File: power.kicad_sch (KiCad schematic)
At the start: 27 parts, among them U21 TPS62A06DRLR, U22 INA228AQDGSRQ1, U23 INA187A2IDBVR

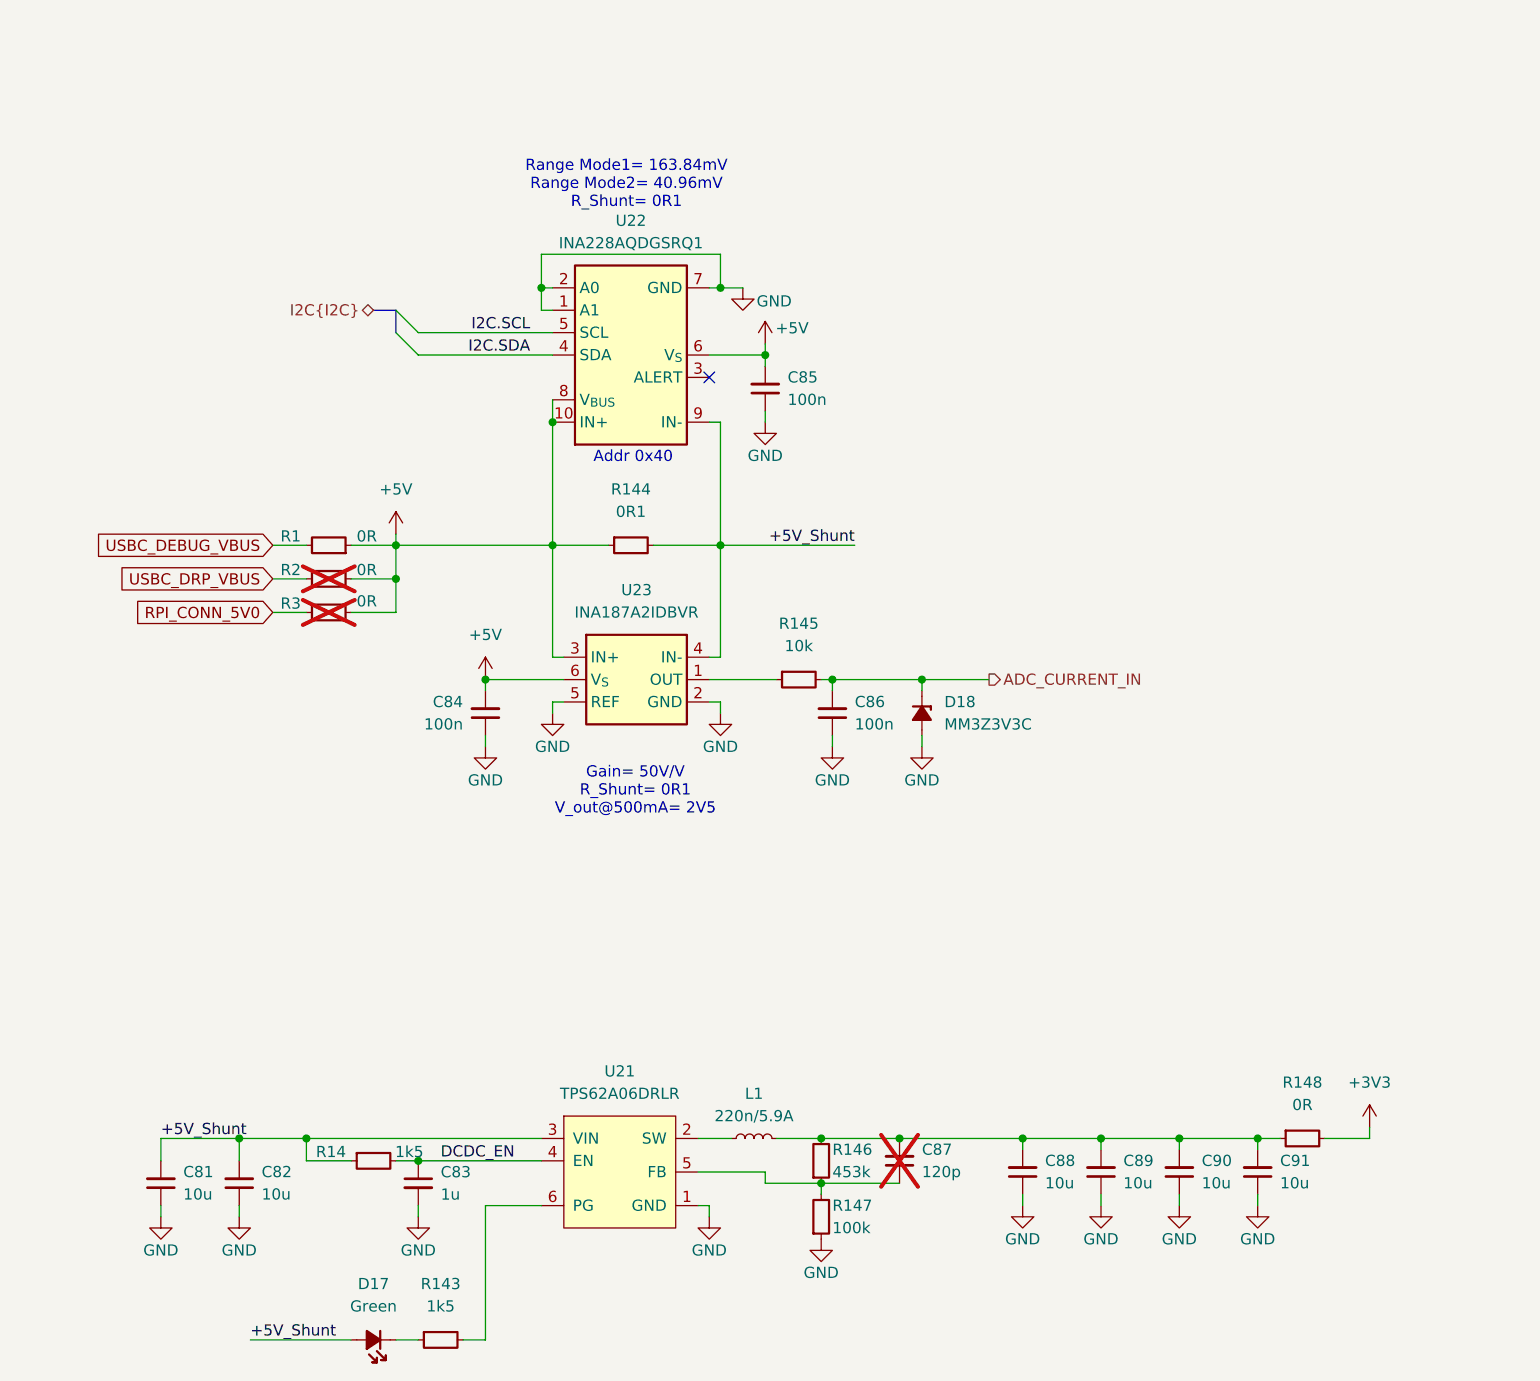
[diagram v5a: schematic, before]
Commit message: [#95036] Solve basic ERCs
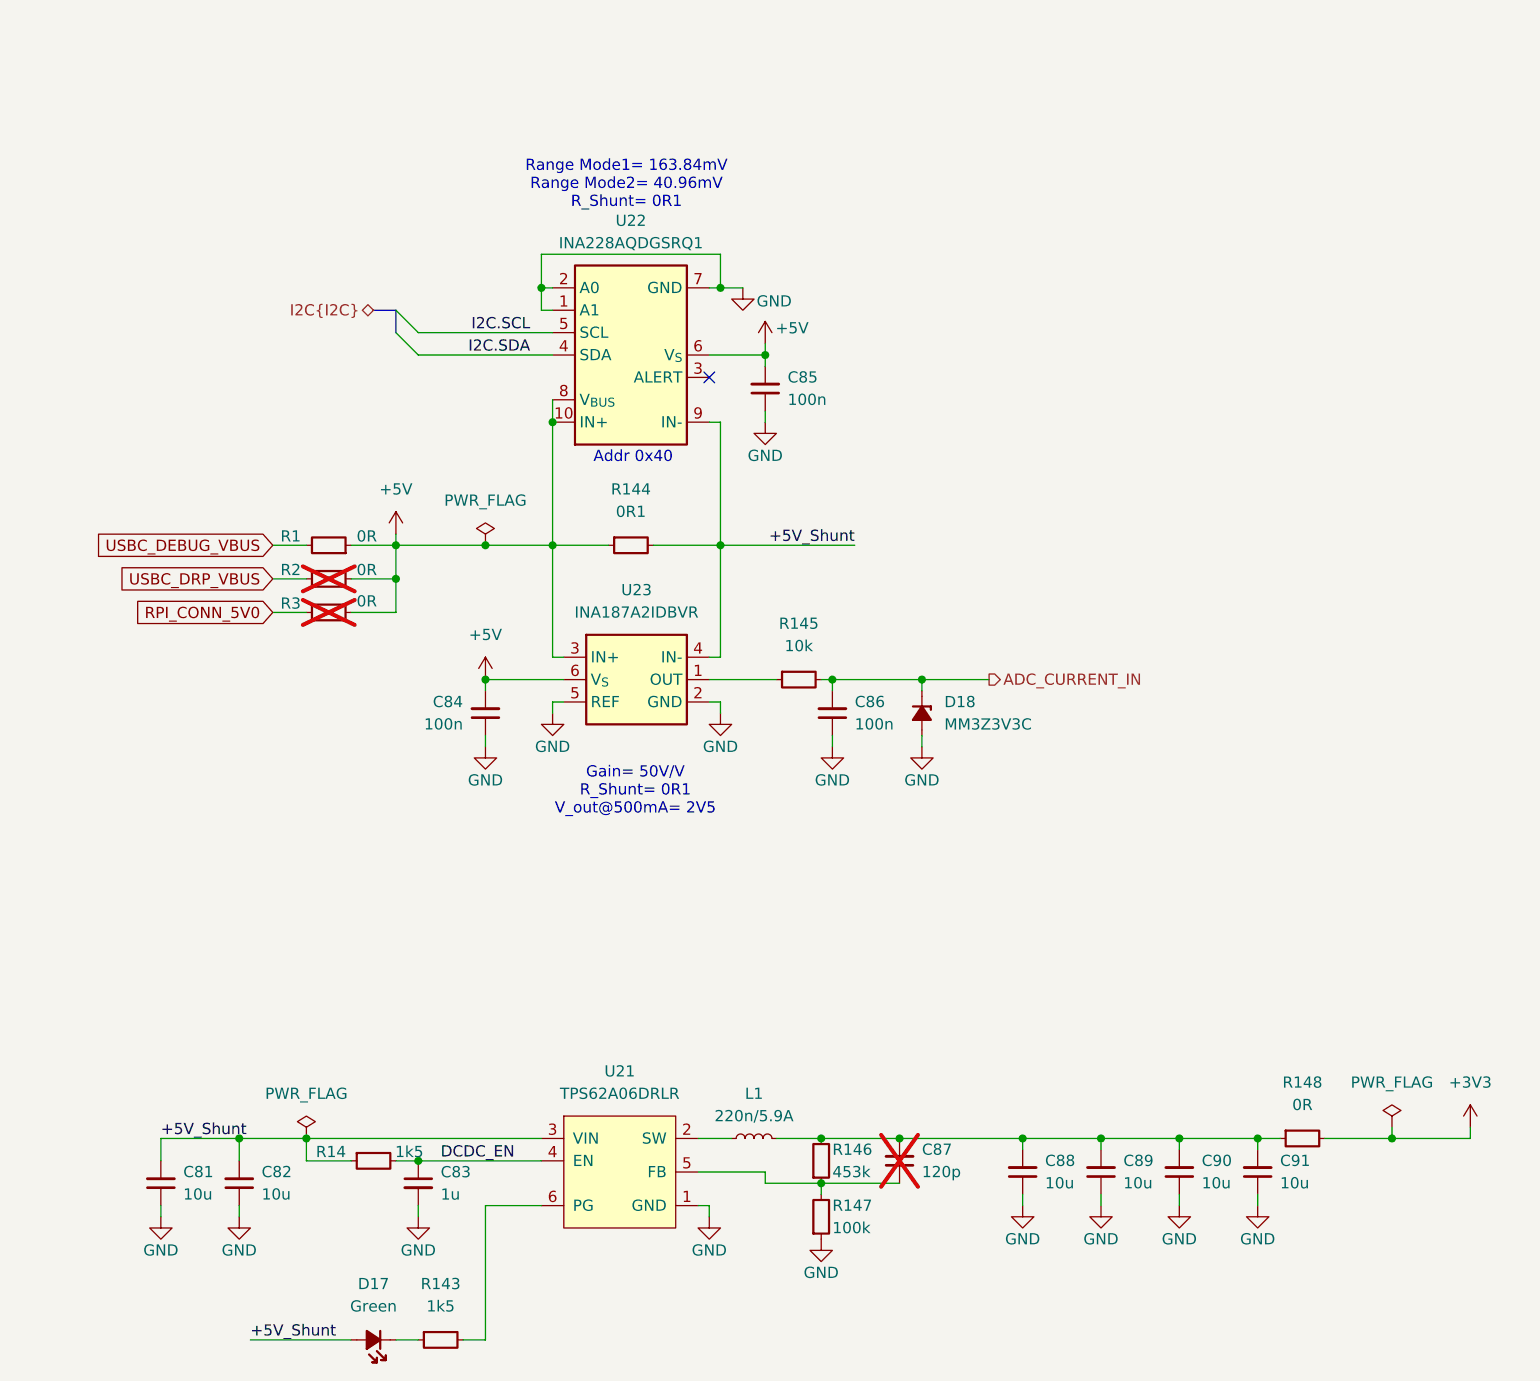
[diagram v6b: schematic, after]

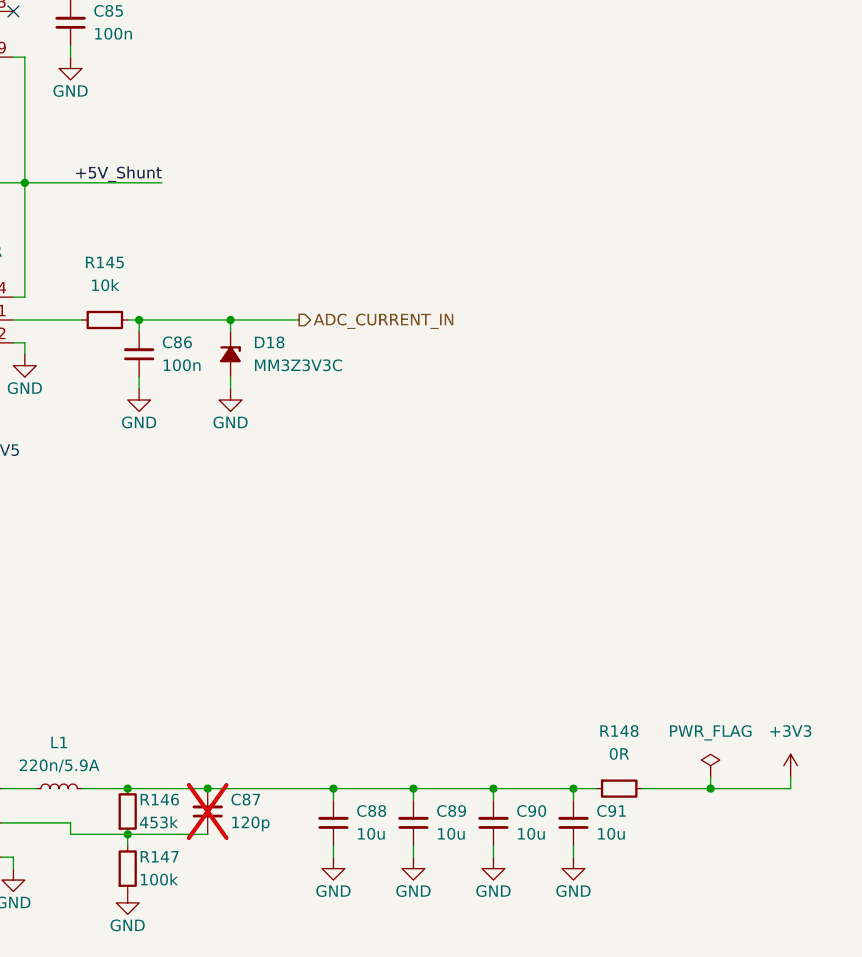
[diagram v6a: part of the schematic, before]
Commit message: [#95036] Add testpoints
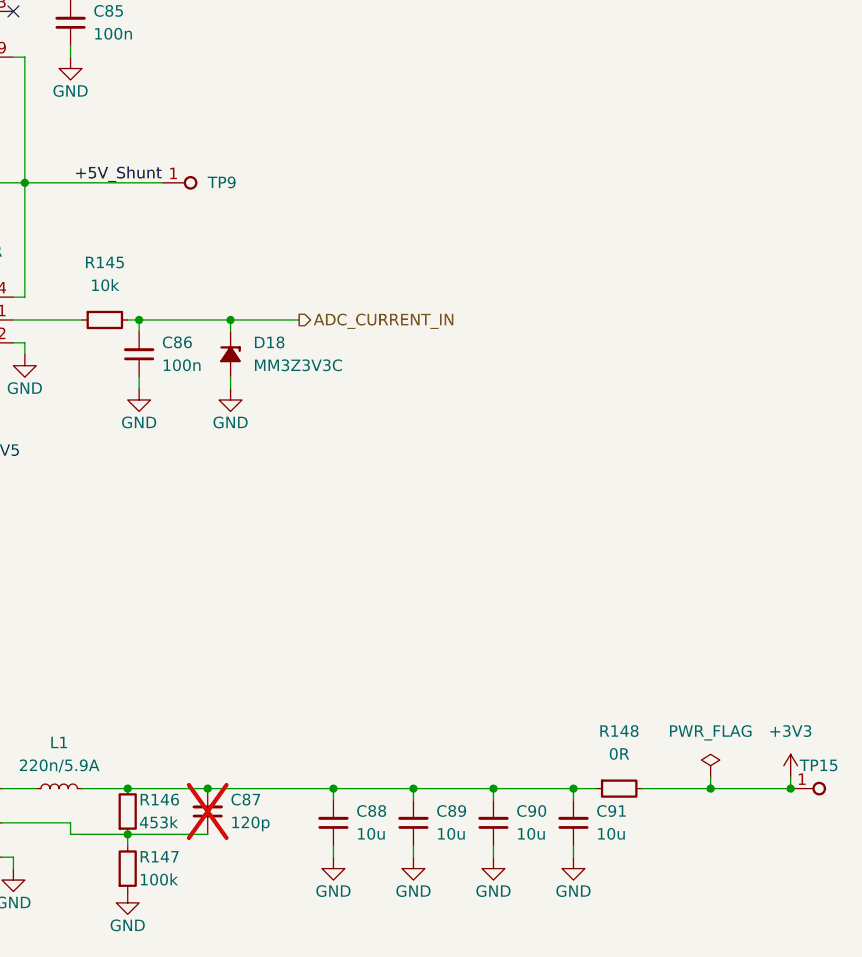
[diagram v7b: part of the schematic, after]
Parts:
- added TP15, TP9: TP_1mm_SMD, antmicro-footprints:TP_SMD_1mm, symbol antmicroTestPoints:TP_1mm_SMD
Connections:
- net +3V3: now also TP15.1
- net +5V_Shunt: now also TP9.1
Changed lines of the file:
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@@
 	)
 	(junction
+		(at 278.13 177.8)
+		(diameter 0)
+		(color 0 0 0 0)
+	)
+	(junction
 		(at 166.37 110.49)
 		(diameter 0)
@@
 	)
 	(symbol
+		(lib_id "antmicroTestPoints:TP_1mm_SMD")
+		(at 278.13 177.8 0)
+		(mirror x)
+		(unit 1)
+		(exclude_from_sim no)
+		(in_bom no)
+		(on_board yes)
+		(dnp no)
+		(property "Reference" "TP15"
+			(at 281.305 175.26 0)
+			(effects
+				(font
+					(size 1.27 1.27)
+					(thickness 0.15)
+				)
+			)
+		)
+		(property "Value" "TP_1mm_SMD"
+			(at 293.37 170.18 0)
+			(effects
+				(font
+					(size 1.27 1.27)
+					(thickness 0.15)
+				)
+				(justify left bottom)
+				(hide yes)
+			)
+		)
+		(property "Footprint" "antmicro-footprints:TP_SMD_1mm"
+			(at 293.37 167.64 0)
+			(effects
+				(font
+					(size 1.27 1.27)
+					(thickness 0.15)
+				)
+				(justify left bottom)
+				(hide yes)
+			)
+		)
+		(property "Datasheet" ""
+			(at 295.91 165.1 0)
+			(effects
+				(font
+					(size 1.27 1.27)
+					(thickness 0.15)
+				)
+				(justify left bottom)
+				(hide yes)
+			)
+		)
+		(property "Description" "Test point 1mm SMD"
+			(at 293.37 157.48 0)
+			(effects
+				(font
+					(size 1.27 1.27)
+				)
+				(justify left bottom)
+				(hide yes)
+			)
+		)
+		(property "MPN" ""
+			(at 278.13 177.8 0)
+			(effects
+				(font
+					(size 1.27 1.27)
+				)
+				(hide yes)
+			)
+		)
+		(property "Manufacturer" ""
+			(at 278.13 177.8 0)
+			(effects
+				(font
+					(size 1.27 1.27)
+				)
+				(hide yes)
+			)
+		)
+		(property "Author" "Antmicro"
+			(at 293.37 162.56 0)
+			(effects
+				(font
+					(size 1.27 1.27)
+					(thickness 0.15)
+				)
+				(justify left bottom)
+				(hide yes)
+			)
+		)
+		(property "License" "Apache-2.0"
+			(at 293.37 160.02 0)
+			(effects
+				(font
+					(size 1.27 1.27)
+					(thickness 0.15)
+				)
+				(justify left bottom)
+				(hide yes)
+			)
+		)
+		(pin "1"
+		)
+		(instances
+			(project "renode-reference-platform"
+				(path "/126ae87b-f292-4372-94ff-ae46971d67ab/3bbe31bb-f2b9-4019-b1b8-20b6749deb1b"
+					(reference "TP15")
+					(unit 1)
+				)
+			)
+		)
+	)
+	(symbol
 		(lib_id "antmicroFixedInductors:L_220n_5.9A_1008")
 		(at 194.31 177.8 0)
@@
 					(unit 1)
 				)
+			)
+		)
+	)
+	(symbol
+		(lib_id "antmicroTestPoints:TP_1mm_SMD")
+		(at 208.28 110.49 0)
+		(unit 1)
+		(exclude_from_sim no)
+		(in_bom no)
+		(on_board yes)
+		(dnp no)
+		(fields_autoplaced yes)
+		(property "Reference" "TP9"
+			(at 213.36 110.49 0)
+			(effects
+				(font
+					(size 1.27 1.27)
+					(thickness 0.15)
+				)
+				(justify left)
+			)
+		)
+		(property "Value" "TP_1mm_SMD"
+			(at 223.52 118.11 0)
+			(effects
+				(font
+					(size 1.27 1.27)
+					(thickness 0.15)
+				)
+				(justify left bottom)
+				(hide yes)
+			)
+		)
+		(property "Footprint" "antmicro-footprints:TP_SMD_1mm"
+			(at 223.52 120.65 0)
+			(effects
+				(font
+					(size 1.27 1.27)
+					(thickness 0.15)
+				)
+				(justify left bottom)
+				(hide yes)
+			)
+		)
+		(property "Datasheet" ""
+			(at 226.06 123.19 0)
+			(effects
+				(font
+					(size 1.27 1.27)
+					(thickness 0.15)
+				)
+				(justify left bottom)
+				(hide yes)
+			)
+		)
+		(property "Description" "Test point 1mm SMD"
+			(at 223.52 130.81 0)
+			(effects
+				(font
+					(size 1.27 1.27)
+				)
+				(justify left bottom)
+				(hide yes)
+			)
+		)
+		(property "MPN" ""
+			(at 208.28 110.49 0)
+			(effects
+				(font
+					(size 1.27 1.27)
+				)
+				(hide yes)
+			)
+		)
+		(property "Manufacturer" ""
+			(at 208.28 110.49 0)
+			(effects
+				(font
+					(size 1.27 1.27)
+				)
+				(hide yes)
+			)
+		)
+		(property "Author" "Antmicro"
+			(at 223.52 125.73 0)
+			(effects
+				(font
+					(size 1.27 1.27)
+					(thickness 0.15)
+				)
+				(justify left bottom)
+				(hide yes)
+			)
+		)
+		(property "License" "Apache-2.0"
+			(at 223.52 128.27 0)
+			(effects
+				(font
+					(size 1.27 1.27)
+					(thickness 0.15)
+				)
+				(justify left bottom)
+				(hide yes)
+			)
+		)
+		(pin "1"
+		)
+		(instances
+			(project "renode-reference-platform"
+				(path "/126ae87b-f292-4372-94ff-ae46971d67ab/3bbe31bb-f2b9-4019-b1b8-20b6749deb1b"
+					(reference "TP9")
+					(unit 1)
+				)
